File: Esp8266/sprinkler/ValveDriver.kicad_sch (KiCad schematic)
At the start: 18 parts, among them J1 Terminal Block 1729128, J2 Terminal Block 1729128, J3 Terminal Block 1729128, Q4 MMBT2222A, Q5 MMBT2222A, Q6 MMBT2222A, U6 MMBT2907A-7-F, U7 MMBT2907A-7-F, U8 MMBT2907A-7-F

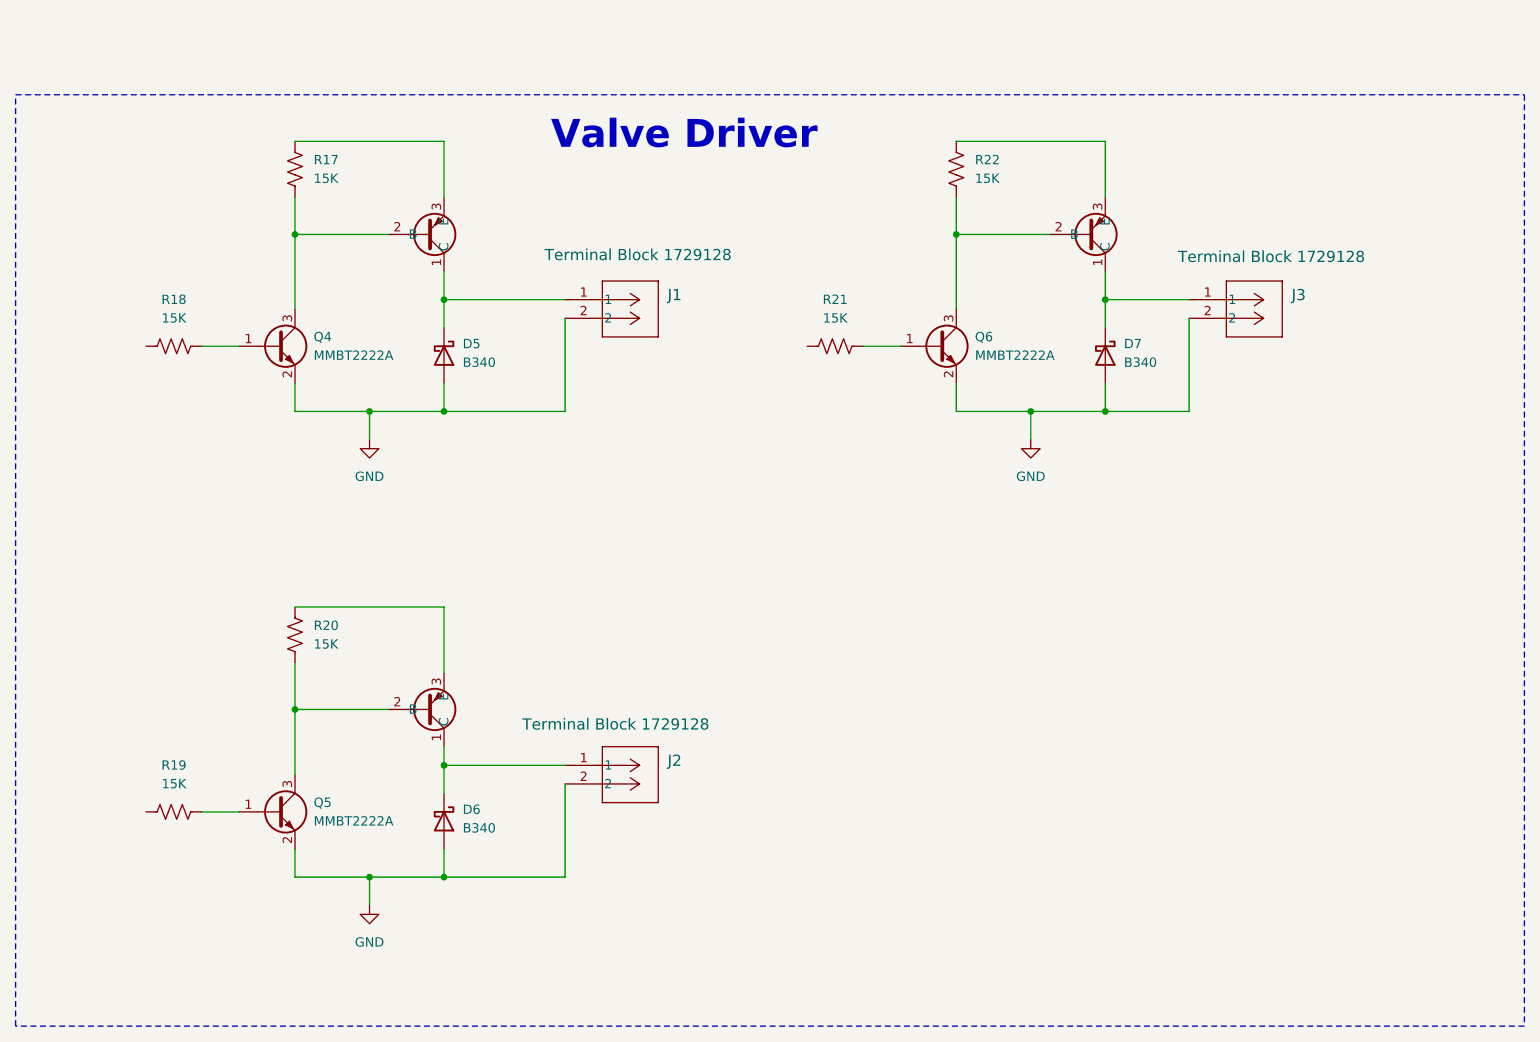
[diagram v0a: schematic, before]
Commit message: Transistor changes
Changed all Bjt transistors to Mosfets
Assign footprints
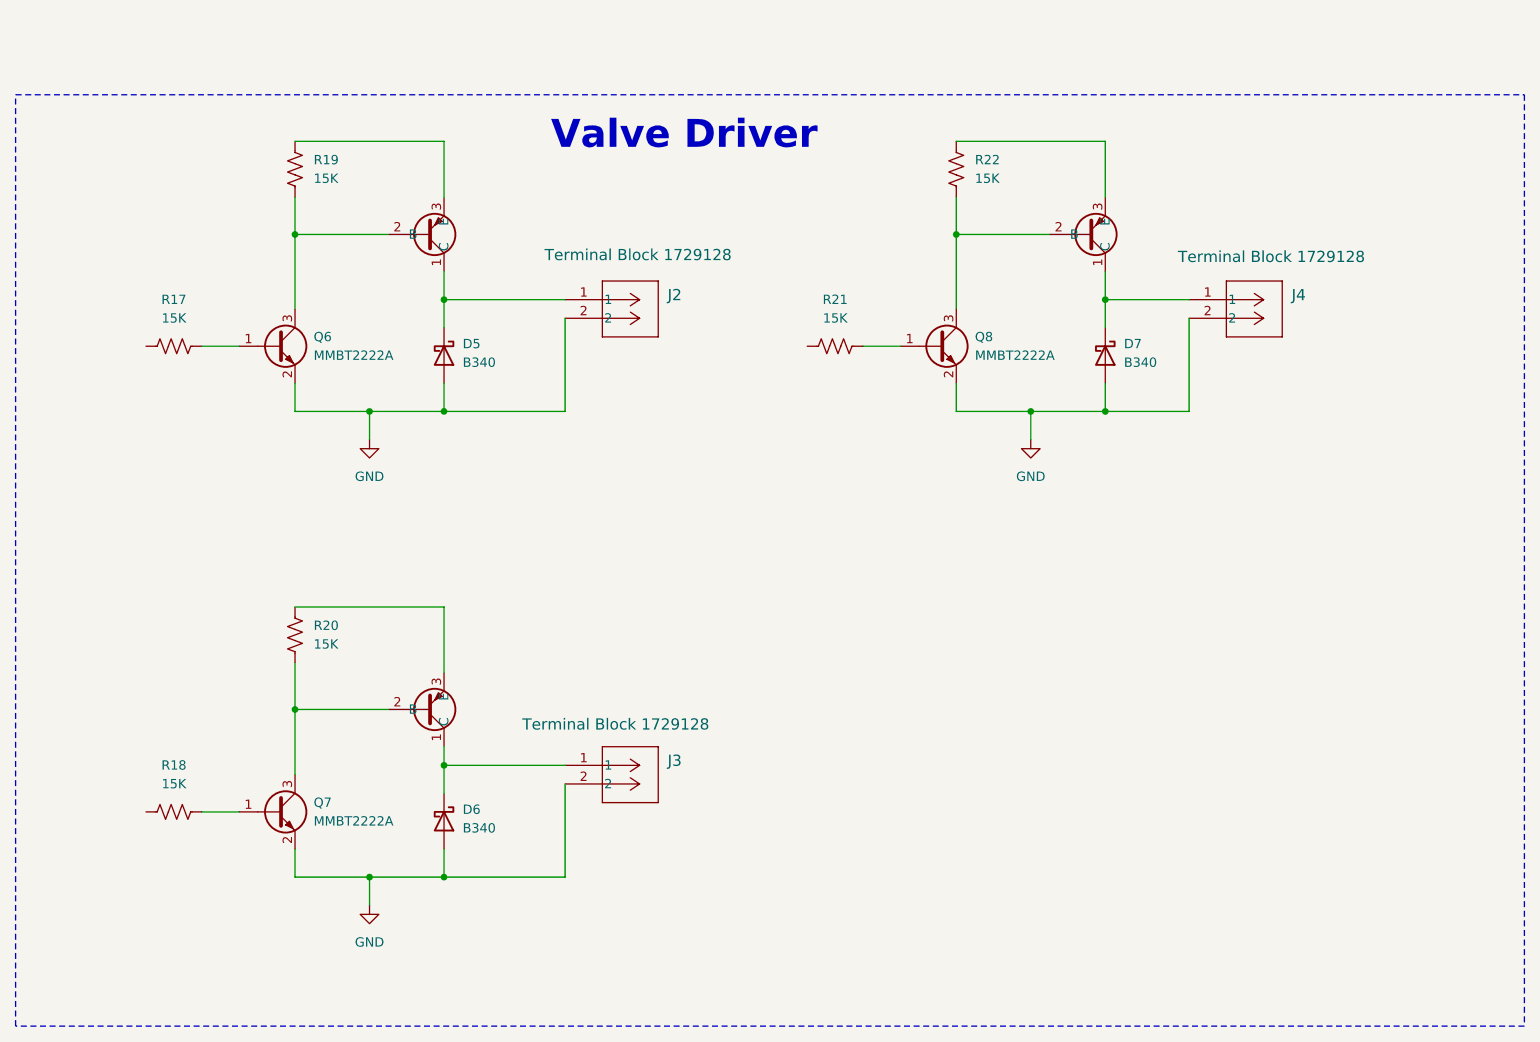
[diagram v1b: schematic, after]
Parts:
- renumbered J1 to J2, J2 to J3, J3 to J4, Q4 to Q6, Q5 to Q7, Q6 to Q8, R18 to R17, R19 to R18, R17 to R19
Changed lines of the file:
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@@
 		(dnp no)
 		(fields_autoplaced yes)
-		(property "Reference" "Q6"
+		(property "Reference" "Q8"
 			(at 173.99 68.58 0)
 			(effects
@@
 			(project "sprinkler"
 				(path "/00ed8740-45a2-4b9d-9104-9548b81da339/d6cea5a1-e7b3-49dc-9ebd-3b743e9b1ddf"
-					(reference "Q6")
+					(reference "Q8")
 					(unit 1)
 				)
@@
 		(dnp no)
 		(fields_autoplaced yes)
-		(property "Reference" "R19"
+		(property "Reference" "R18"
 			(at 64.77 127 90)
 			(effects
@@
 			(project "sprinkler"
 				(path "/00ed8740-45a2-4b9d-9104-9548b81da339/d6cea5a1-e7b3-49dc-9ebd-3b743e9b1ddf"
-					(reference "R19")
+					(reference "R18")
 					(unit 1)
 				)
@@
 		(on_board yes)
 		(dnp no)
-		(property "Reference" "J1"
+		(property "Reference" "J2"
 			(at 132.08 62.8649 0)
 			(effects
@@
 			(project ""
 				(path "/00ed8740-45a2-4b9d-9104-9548b81da339/d6cea5a1-e7b3-49dc-9ebd-3b743e9b1ddf"
-					(reference "J1")
+					(reference "J2")
 					(unit 1)
 				)
@@
 		(dnp no)
 		(fields_autoplaced yes)
-		(property "Reference" "#PWR024"
+		(property "Reference" "#PWR026"
 			(at 91.44 88.9 0)
 			(effects
@@
 			(project ""
 				(path "/00ed8740-45a2-4b9d-9104-9548b81da339/d6cea5a1-e7b3-49dc-9ebd-3b743e9b1ddf"
-					(reference "#PWR024")
+					(reference "#PWR026")
 					(unit 1)
 				)
@@
 		(on_board yes)
 		(dnp no)
-		(property "Reference" "J3"
+		(property "Reference" "J4"
 			(at 217.17 62.8649 0)
 			(effects
@@
 			(project ""
 				(path "/00ed8740-45a2-4b9d-9104-9548b81da339/d6cea5a1-e7b3-49dc-9ebd-3b743e9b1ddf"
-					(reference "J3")
+					(reference "J4")
 					(unit 1)
 				)
@@
 		(dnp no)
 		(fields_autoplaced yes)
-		(property "Reference" "Q5"
+		(property "Reference" "Q7"
 			(at 83.82 132.08 0)
 			(effects
@@
 			(project "sprinkler"
 				(path "/00ed8740-45a2-4b9d-9104-9548b81da339/d6cea5a1-e7b3-49dc-9ebd-3b743e9b1ddf"
-					(reference "Q5")
+					(reference "Q7")
 					(unit 1)
 				)
@@
 		(dnp no)
 		(fields_autoplaced yes)
-		(property "Reference" "#PWR026"
+		(property "Reference" "#PWR028"
 			(at 181.61 88.9 0)
 			(effects
@@
 			(project "sprinkler"
 				(path "/00ed8740-45a2-4b9d-9104-9548b81da339/d6cea5a1-e7b3-49dc-9ebd-3b743e9b1ddf"
-					(reference "#PWR026")
+					(reference "#PWR028")
 					(unit 1)
 				)
@@
 		(on_board yes)
 		(dnp no)
-		(property "Reference" "J2"
+		(property "Reference" "J3"
 			(at 132.08 126.3649 0)
 			(effects
@@
 			(project ""
 				(path "/00ed8740-45a2-4b9d-9104-9548b81da339/d6cea5a1-e7b3-49dc-9ebd-3b743e9b1ddf"
-					(reference "J2")
+					(reference "J3")
 					(unit 1)
 				)
@@
 		(dnp no)
 		(fields_autoplaced yes)
-		(property "Reference" "R17"
+		(property "Reference" "R19"
 			(at 83.82 44.45 0)
 			(effects
@@
 			(project ""
 				(path "/00ed8740-45a2-4b9d-9104-9548b81da339/d6cea5a1-e7b3-49dc-9ebd-3b743e9b1ddf"
-					(reference "R17")
+					(reference "R19")
 					(unit 1)
 				)
@@
 		(dnp no)
 		(fields_autoplaced yes)
-		(property "Reference" "R18"
+		(property "Reference" "R17"
 			(at 64.77 63.5 90)
 			(effects
@@
 			(project ""
 				(path "/00ed8740-45a2-4b9d-9104-9548b81da339/d6cea5a1-e7b3-49dc-9ebd-3b743e9b1ddf"
-					(reference "R18")
+					(reference "R17")
 					(unit 1)
 				)
@@
 		(dnp no)
 		(fields_autoplaced yes)
-		(property "Reference" "Q4"
+		(property "Reference" "Q6"
 			(at 83.82 68.58 0)
 			(effects
@@
 			(project ""
 				(path "/00ed8740-45a2-4b9d-9104-9548b81da339/d6cea5a1-e7b3-49dc-9ebd-3b743e9b1ddf"
-					(reference "Q4")
+					(reference "Q6")
 					(unit 1)
 				)
@@
 		(dnp no)
 		(fields_autoplaced yes)
-		(property "Reference" "#PWR025"
+		(property "Reference" "#PWR027"
 			(at 91.44 152.4 0)
 			(effects
@@
 			(project "sprinkler"
 				(path "/00ed8740-45a2-4b9d-9104-9548b81da339/d6cea5a1-e7b3-49dc-9ebd-3b743e9b1ddf"
-					(reference "#PWR025")
-					(unit 1)
-				)
+					(reference "#PWR027")
+					(unit 1)
+				)

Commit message: Update connections
Connect Micro controller inputs and outputs
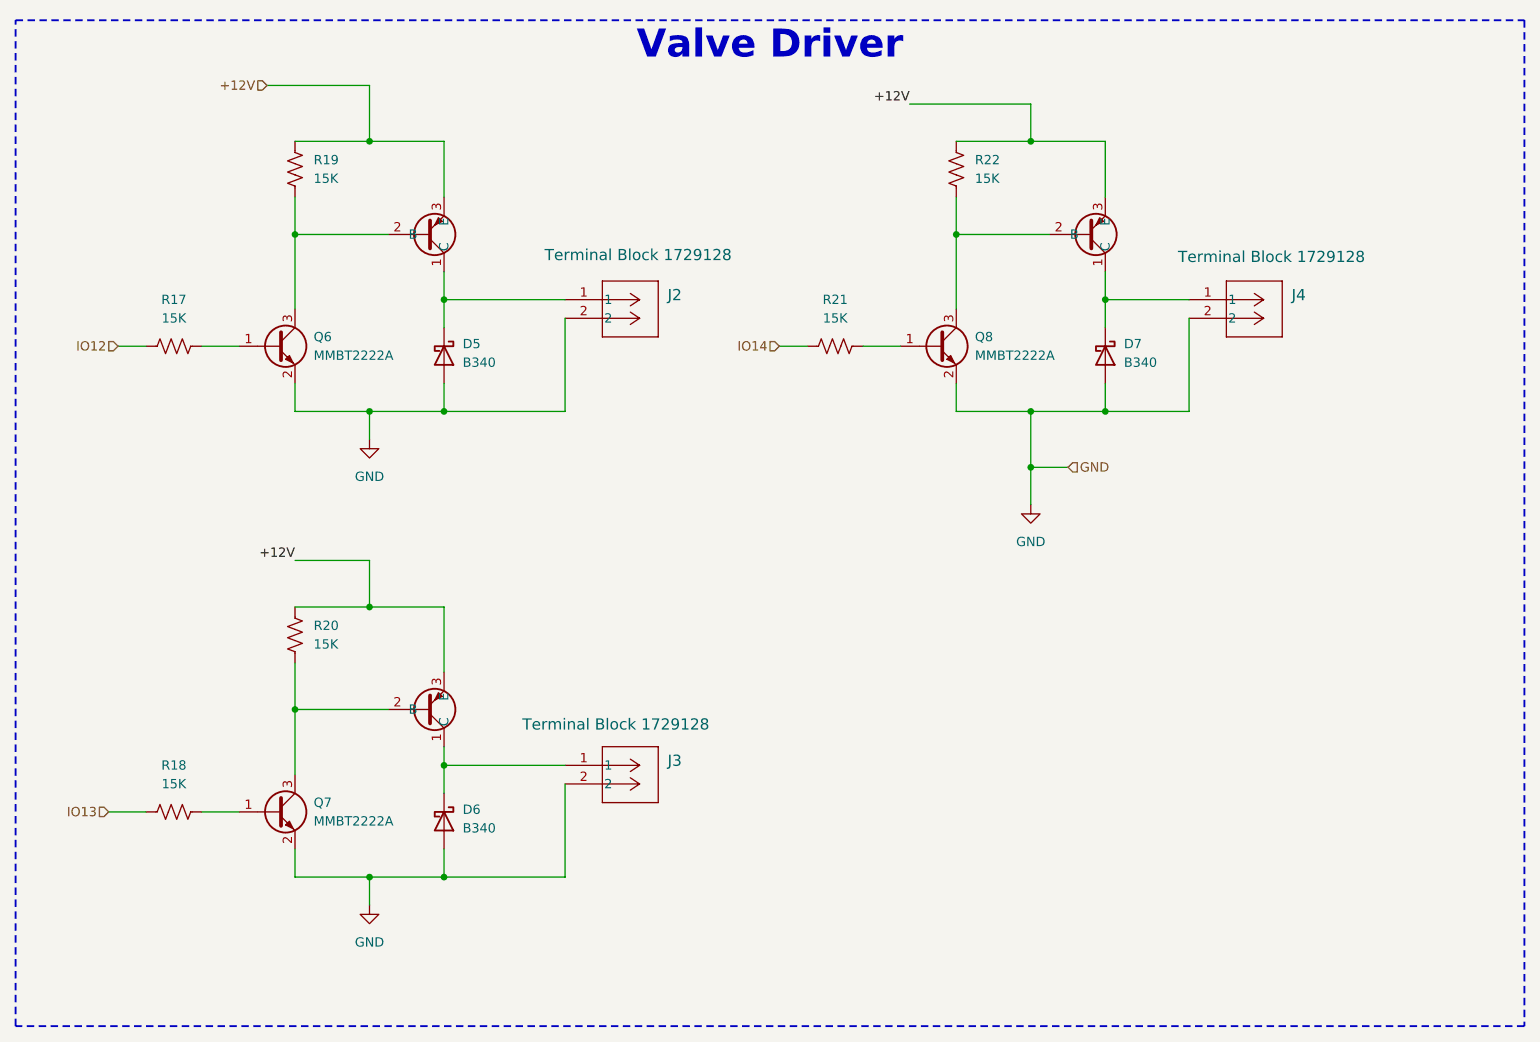
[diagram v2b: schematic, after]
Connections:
- net +12V: now reaches R22.1, U8.3 (E)
- net +12V: now also R19.1, R20.1, U6.3 (E), U7.3 (E)
- net IO13: now reaches R18.1
- net IO12: now reaches R17.1
- net IO14: now reaches R21.1
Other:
- note removed: "Valve Driver"
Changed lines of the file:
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@@
 	(generator_version "9.0")
 	(paper "A4")
-	(text "Valve Driver"
+	(text_box "Valve Driver"
 		(exclude_from_sim no)
-		(at 134.366 41.148 0)
+		(at 43.18 25.4 0)
+		(size 205.74 137.16)
+		(margins 0.9525 0.9525 0.9525 0.9525)
+		(stroke
+			(width 0.254)
+			(type dash_dot_dot)
+		)
+		(fill
+			(type none)
+		)
 		(effects
 			(font
@@
 				(bold yes)
 			)
-		)
-	)
-	(text_box ""
-		(exclude_from_sim no)
-		(at 43.18 35.56 0)
-		(size 205.74 127)
-		(margins 0.9525 0.9525 0.9525 0.9525)
-		(stroke
-			(width 0)
-			(type dash_dot_dot)
-		)
-		(fill
-			(type none)
-		)
-		(effects
-			(font
-				(size 1.27 1.27)
-			)
-			(justify left top)
+			(justify top)
 		)
 	)
@@
 	)
 	(junction
+		(at 181.61 41.91)
+		(diameter 0)
+		(color 0 0 0 0)
+	)
+	(junction
+		(at 181.61 86.36)
+		(diameter 0)
+		(color 0 0 0 0)
+	)
+	(junction
 		(at 171.45 54.61)
 		(diameter 0)
@@
 	)
 	(junction
+		(at 91.44 105.41)
+		(diameter 0)
+		(color 0 0 0 0)
+	)
+	(junction
+		(at 91.44 41.91)
+		(diameter 0)
+		(color 0 0 0 0)
+	)
+	(junction
 		(at 191.77 78.74)
 		(diameter 0)
@@
 	(wire
 		(pts
+			(xy 165.1 36.83) (xy 181.61 36.83)
+		)
+		(stroke
+			(width 0)
+			(type default)
+		)
+	)
+	(wire
+		(pts
+			(xy 91.44 105.41) (xy 101.6 105.41)
+		)
+		(stroke
+			(width 0)
+			(type default)
+		)
+	)
+	(wire
+		(pts
 			(xy 81.28 78.74) (xy 91.44 78.74)
 		)
@@
 	(wire
 		(pts
-			(xy 81.28 41.91) (xy 101.6 41.91)
+			(xy 181.61 36.83) (xy 181.61 41.91)
+		)
+		(stroke
+			(width 0)
+			(type default)
+		)
+	)
+	(wire
+		(pts
+			(xy 81.28 41.91) (xy 91.44 41.91)
 		)
 		(stroke
@@
 	(wire
 		(pts
+			(xy 181.61 86.36) (xy 186.69 86.36)
+		)
+		(stroke
+			(width 0)
+			(type default)
+		)
+	)
+	(wire
+		(pts
 			(xy 91.44 78.74) (xy 101.6 78.74)
 		)
@@
 	(wire
 		(pts
-			(xy 181.61 78.74) (xy 181.61 82.55)
+			(xy 147.32 69.85) (xy 151.13 69.85)
+		)
+		(stroke
+			(width 0)
+			(type default)
+		)
+	)
+	(wire
+		(pts
+			(xy 181.61 78.74) (xy 181.61 86.36)
+		)
+		(stroke
+			(width 0)
+			(type default)
+		)
+	)
+	(wire
+		(pts
+			(xy 57.15 69.85) (xy 60.96 69.85)
+		)
+		(stroke
+			(width 0)
+			(type default)
+		)
+	)
+	(wire
+		(pts
+			(xy 181.61 86.36) (xy 181.61 91.44)
 		)
 		(stroke
@@
 	(wire
 		(pts
-			(xy 81.28 105.41) (xy 101.6 105.41)
+			(xy 91.44 41.91) (xy 101.6 41.91)
+		)
+		(stroke
+			(width 0)
+			(type default)
+		)
+	)
+	(wire
+		(pts
+			(xy 81.28 105.41) (xy 91.44 105.41)
 		)
 		(stroke
@@
 	(wire
 		(pts
+			(xy 55.88 133.35) (xy 60.96 133.35)
+		)
+		(stroke
+			(width 0)
+			(type default)
+		)
+	)
+	(wire
+		(pts
 			(xy 184.15 54.61) (xy 171.45 54.61)
 		)
@@
 	(wire
 		(pts
+			(xy 91.44 99.06) (xy 91.44 105.41)
+		)
+		(stroke
+			(width 0)
+			(type default)
+		)
+	)
+	(wire
+		(pts
 			(xy 101.6 142.24) (xy 101.6 138.43)
 		)
@@
 	(wire
 		(pts
+			(xy 81.28 99.06) (xy 91.44 99.06)
+		)
+		(stroke
+			(width 0)
+			(type default)
+		)
+	)
+	(wire
+		(pts
 			(xy 81.28 49.53) (xy 81.28 54.61)
 		)
@@
 	(wire
 		(pts
+			(xy 181.61 41.91) (xy 191.77 41.91)
+		)
+		(stroke
+			(width 0)
+			(type default)
+		)
+	)
+	(wire
+		(pts
 			(xy 101.6 124.46) (xy 101.6 127)
 		)
@@
 	(wire
 		(pts
+			(xy 91.44 34.29) (xy 91.44 41.91)
+		)
+		(stroke
+			(width 0)
+			(type default)
+		)
+	)
+	(wire
+		(pts
 			(xy 101.6 78.74) (xy 101.6 74.93)
 		)
@@
 	(wire
 		(pts
-			(xy 171.45 41.91) (xy 191.77 41.91)
+			(xy 171.45 41.91) (xy 181.61 41.91)
 		)
 		(stroke
@@
 	(wire
 		(pts
+			(xy 77.47 34.29) (xy 91.44 34.29)
+		)
+		(stroke
+			(width 0)
+			(type default)
+		)
+	)
+	(wire
+		(pts
 			(xy 81.28 142.24) (xy 91.44 142.24)
 		)
@@
 			(width 0)
 			(type default)
+		)
+	)
+	(label "+12V"
+		(at 81.28 99.06 180)
+		(effects
+			(font
+				(size 1.27 1.27)
+			)
+			(justify right bottom)
+		)
+	)
+	(label "+12V"
+		(at 165.1 36.83 180)
+		(effects
+			(font
+				(size 1.27 1.27)
+			)
+			(justify right bottom)
+		)
+	)
+	(hierarchical_label "GND"
+		(shape input)
+		(at 186.69 86.36 0)
+		(effects
+			(font
+				(size 1.27 1.27)
+			)
+			(justify left)
+		)
+	)
+	(hierarchical_label "IO14"
+		(shape input)
+		(at 147.32 69.85 180)
+		(effects
+			(font
+				(size 1.27 1.27)
+			)
+			(justify right)
+		)
+	)
+	(hierarchical_label "IO13"
+		(shape input)
+		(at 55.88 133.35 180)
+		(effects
+			(font
+				(size 1.27 1.27)
+			)
+			(justify right)
+		)
+	)
+	(hierarchical_label "IO12"
+		(shape input)
+		(at 57.15 69.85 180)
+		(effects
+			(font
+				(size 1.27 1.27)
+			)
+			(justify right)
+		)
+	)
+	(hierarchical_label "+12V"
+		(shape input)
+		(at 77.47 34.29 180)
+		(effects
+			(font
+				(size 1.27 1.27)
+			)
+			(justify right)
 		)
 	)
@@
 	(symbol
 		(lib_id "power:GND")
-		(at 181.61 82.55 0)
+		(at 181.61 91.44 0)
 		(unit 1)
 		(exclude_from_sim no)
@@
 		(fields_autoplaced yes)
 		(property "Reference" "#PWR028"
-			(at 181.61 88.9 0)
+			(at 181.61 97.79 0)
 			(effects
 				(font
@@
 		)
 		(property "Value" "GND"
-			(at 181.61 87.63 0)
+			(at 181.61 96.52 0)
 			(effects
 				(font
@@
 		)
 		(property "Footprint" ""
-			(at 181.61 82.55 0)
+			(at 181.61 91.44 0)
 			(effects
 				(font
@@
 		)
 		(property "Datasheet" ""
-			(at 181.61 82.55 0)
+			(at 181.61 91.44 0)
 			(effects
 				(font
@@
 		)
 		(property "Description" "Power symbol creates a global label with name \"GND\" , ground"
-			(at 181.61 82.55 0)
-			(effects
-				(font
+			(at 181.61 91.44 0)
+			(effects
+				(font
